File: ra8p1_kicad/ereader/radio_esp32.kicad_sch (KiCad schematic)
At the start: 22 parts, among them U3 ESP32-C6-WROOM-1-N8, U4 TPS22917DBVT, U5 TXU0304PWR, U6 TPS389001DSET, U7 SN74LVC1G97DBVR

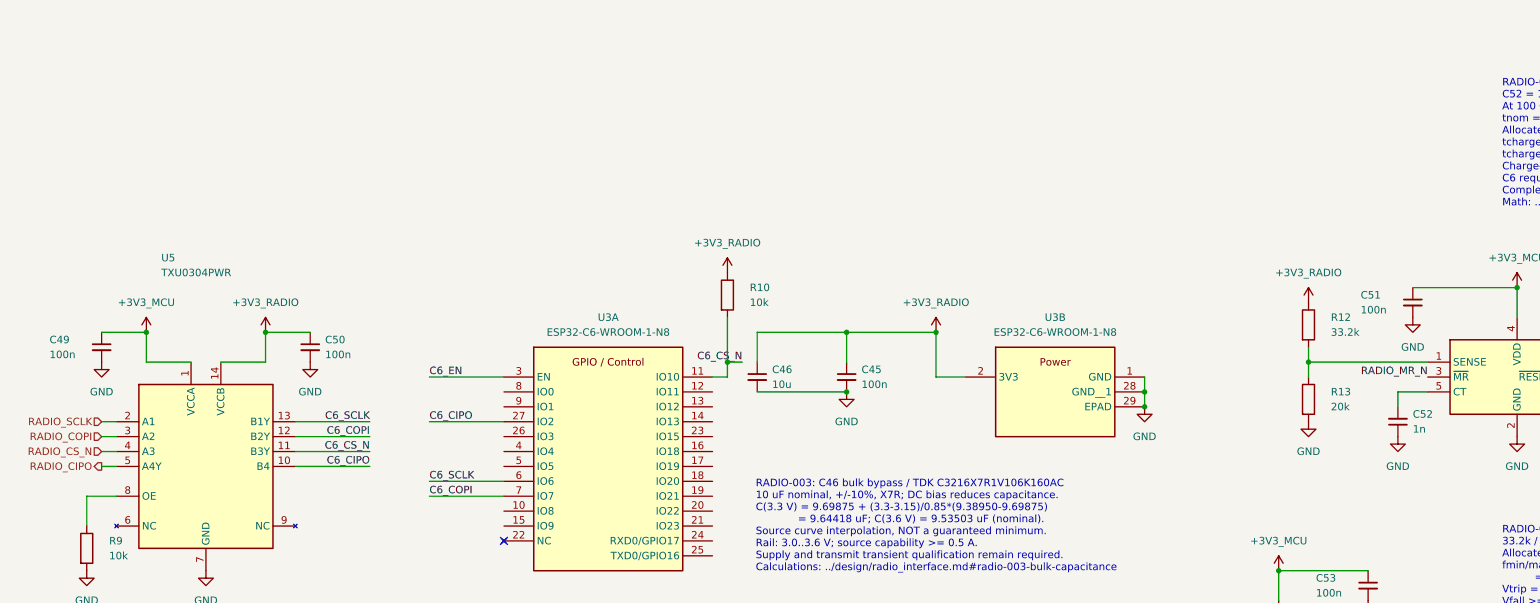
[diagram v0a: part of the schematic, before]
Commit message: Add radio SPI enable arbitration and linked DC calculations
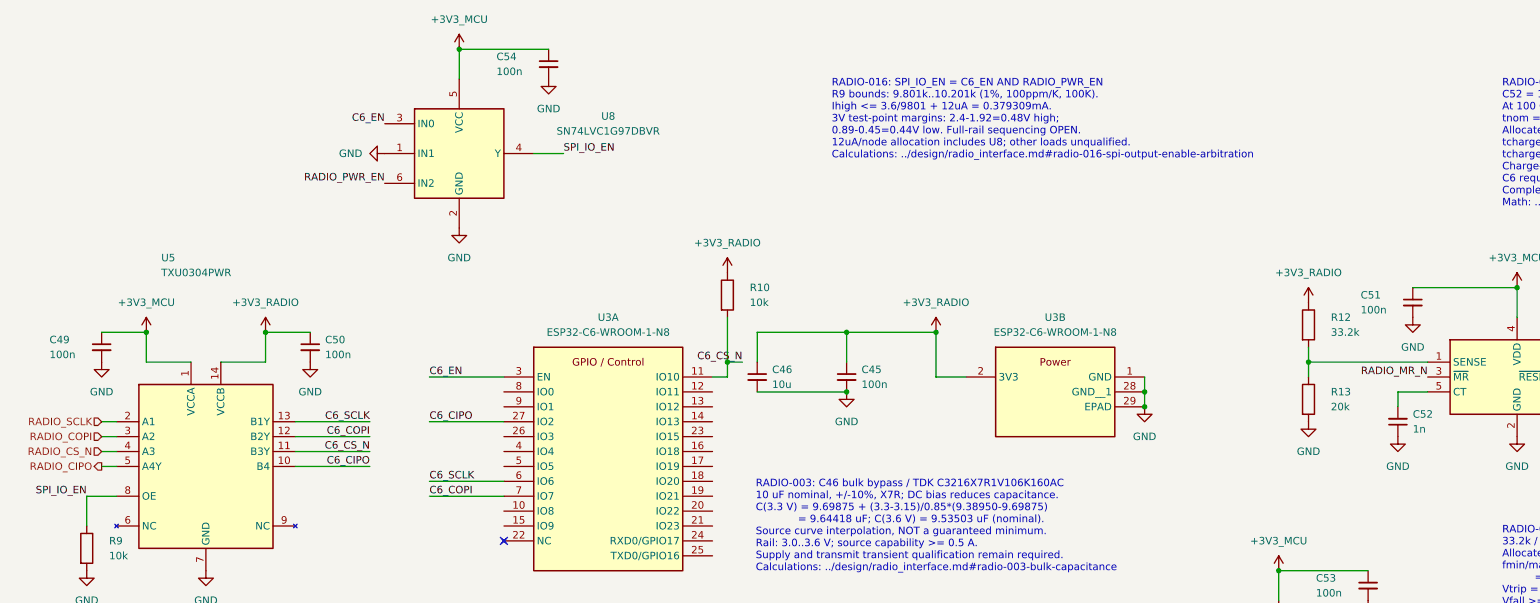
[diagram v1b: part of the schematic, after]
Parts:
- added C54: 100n, symbol Device:C_Small
- added U8: SN74LVC1G97DBVR, symbol 74xGxx:74LVC1G97
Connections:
- net +3V3_MCU: now also C54.1, U8.5 (VCC)
- net C6_EN: now also U8.3 (IN0)
- net GND: now also C54.2, U8.1 (IN1), U8.2 (GND)
- net RADIO_PWR_EN: now also U8.6 (IN2)
- net SPI_IO_EN: now reaches R9.1, U5.8 (OE)
- net SPI_IO_EN: now also U8.4 (Y)
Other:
- note added: "RADIO-016: SPI_IO_EN = C6_EN AND RADIO_PWR_EN R9 bounds: 9.801k..10.201k (1%, 100ppm/K, 100K). Ihigh <= 3.6/9801 + 12uA = 0.379309mA. 3V test-point margins: 2.4-1.92=0.48V high; 0.89-0.45=0.44V low. Full-rail sequencing OPEN. 12uA/node allocation includes U8; other loads unqualified. Calculations: ../design/radio_interface.md#radio-016-spi-output-enable-arbitration"

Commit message: Add ESP32 boot and debug strap bias with verified calculations
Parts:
- added R15, R16, R17: 10k, symbol Device:R
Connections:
- net +3V3_RADIO: now also R15.1, R16.1, R17.1
- net C6_GPIO8: now reaches U3.10 (IO8)
- net C6_GPIO8: now also R15.2
- net C6_BOOT_N: now reaches U3.15 (IO9)
- net C6_BOOT_N: now also R16.2
- net C6_GPIO15: now reaches U3.23 (IO15)
- net C6_GPIO15: now also R17.2
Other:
- note added: "RADIO-017: R15/R16/R17 boot/debug strap pull-ups to switched radio rail. Flash boot: GPIO9=1. Download: GPIO8=1, GPIO9=0; recovery driver not yet fitted. GPIO15=1 selects USB JTAG with applicable eFuses; retain straps >=3ms after EN rises. Rmin/max=10k*(1+/-1%)*(1+/-100ppm/K*100K)=9801/10201 ohm. At 3.3V: Vhigh>=3.3-12uA*10201=3.177588V; VIH=2.475V; margin=0.702588V. External low-state current<=3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"

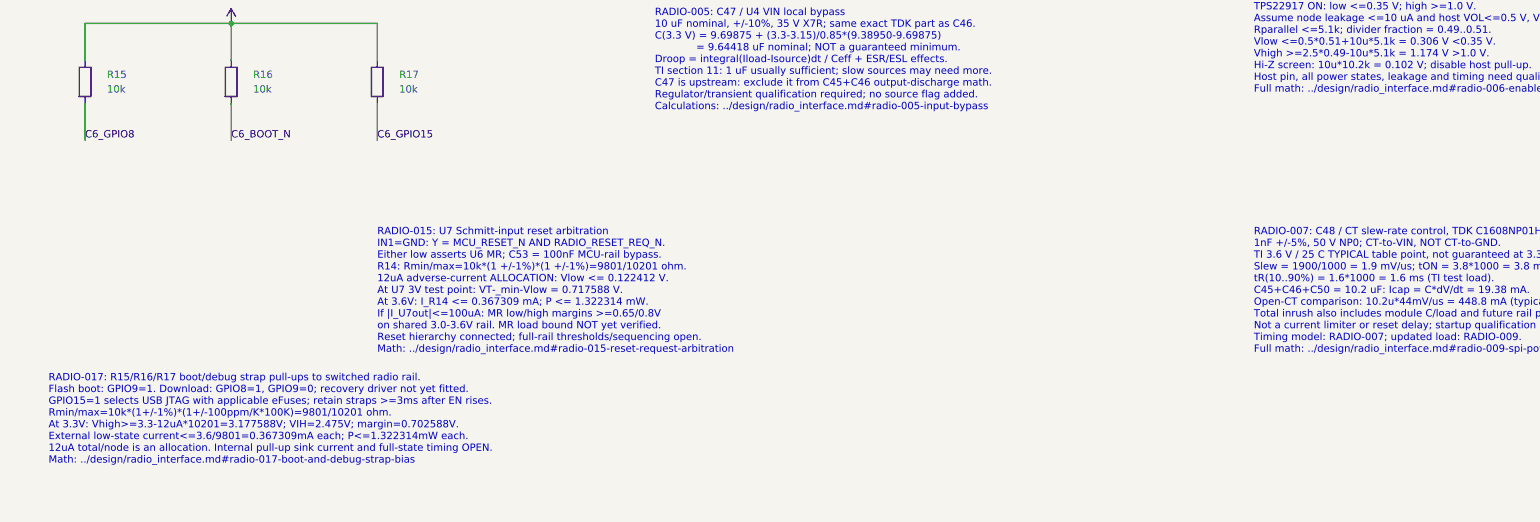
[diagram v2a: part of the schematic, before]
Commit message: Add sourced manual radio BOOT switch and recovery timing contract
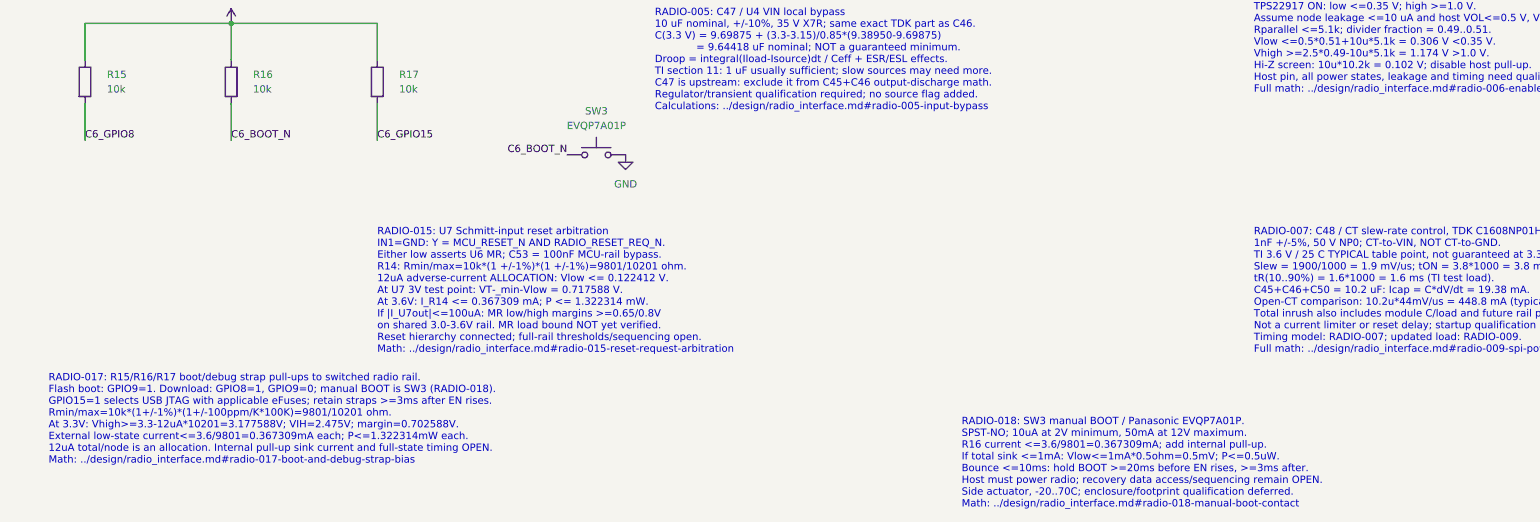
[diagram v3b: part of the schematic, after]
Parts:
- added SW3: EVQP7A01P, symbol Switch:SW_Push
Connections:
- net C6_BOOT_N: now also SW3.1
- net GND: now also SW3.2
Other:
- note added: "RADIO-017: R15/R16/R17 boot/debug strap pull-ups to switched radio rail. Flash boot: GPIO9=1. Download: GPIO8=1, GPIO9=0; manual BOOT is SW3 (RADIO-018). GPIO15=1 selects USB JTAG with applicable eFuses; retain straps >=3ms after EN rises. Rmin/max=10k*(1+/-1%)*(1+/-100ppm/K*100K)=9801/10201 ohm. At 3.3V: Vhigh>=3.3-12uA*10201=3.177588V; VIH=2.475V; margin=0.702588V. External low-state current<=3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"
- note added: "RADIO-018: SW3 manual BOOT / Panasonic EVQP7A01P. SPST-NO; 10uA at 2V minimum, 50mA at 12V maximum. R16 current <=3.6/9801=0.367309mA; add internal pull-up. If total sink <=1mA: Vlow<=1mA*0.5ohm=0.5mV; P<=0.5uW. Bounce <=10ms: hold BOOT >=20ms before EN rises, >=3ms after. Host must power radio; recovery data access/sequencing remain OPEN. Side actuator, -20..70C; enclosure/footprint qualificatio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"
- note removed: "RADIO-017: R15/R16/R17 boot/debug strap pull-ups to switched radio rail. Flash boot: GPIO9=1. Download: GPIO8=1, GPIO9=0; recovery driver not yet fitted. GPIO15=1 selects USB JTAG with applicable eFuses; retain straps >=3ms after EN rises. Rmin/max=10k*(1+/-1%)*(1+/-100ppm/K*100K)=9801/10201 ohm. At 3.3V: Vhigh>=3.3-12uA*10201=3.177588V; VIH=2.475V; margin=0.702588V. External low-state current<=3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"

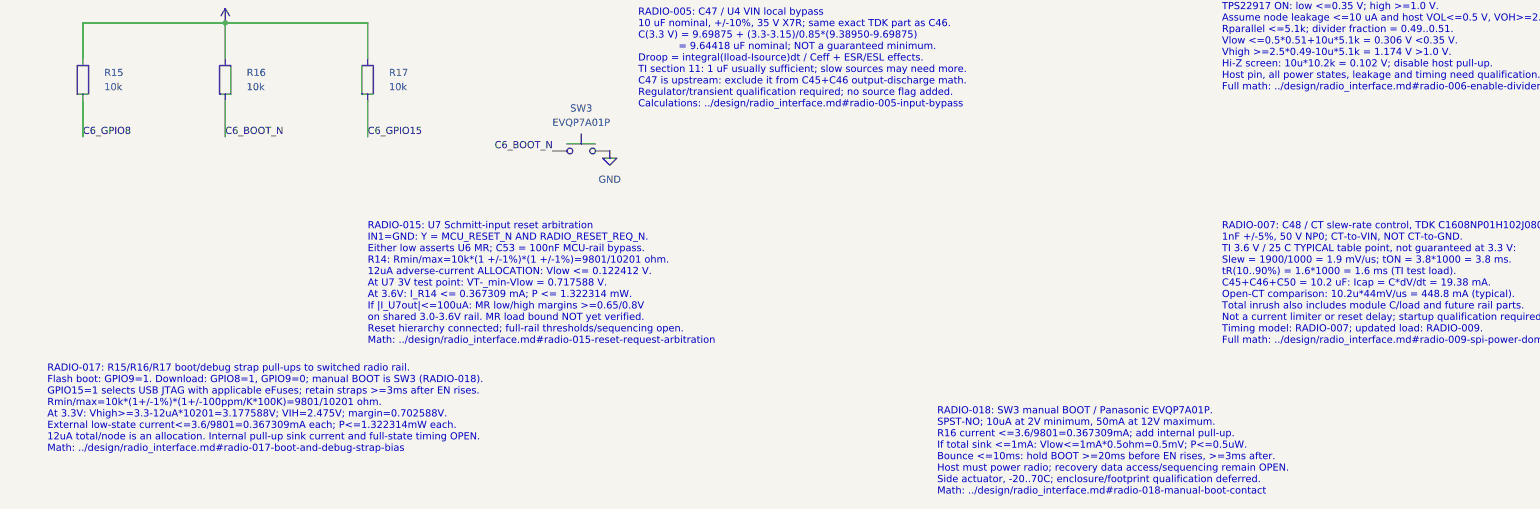
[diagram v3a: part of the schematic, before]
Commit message: Replace engineering BOOT and reset switches with internal service pads
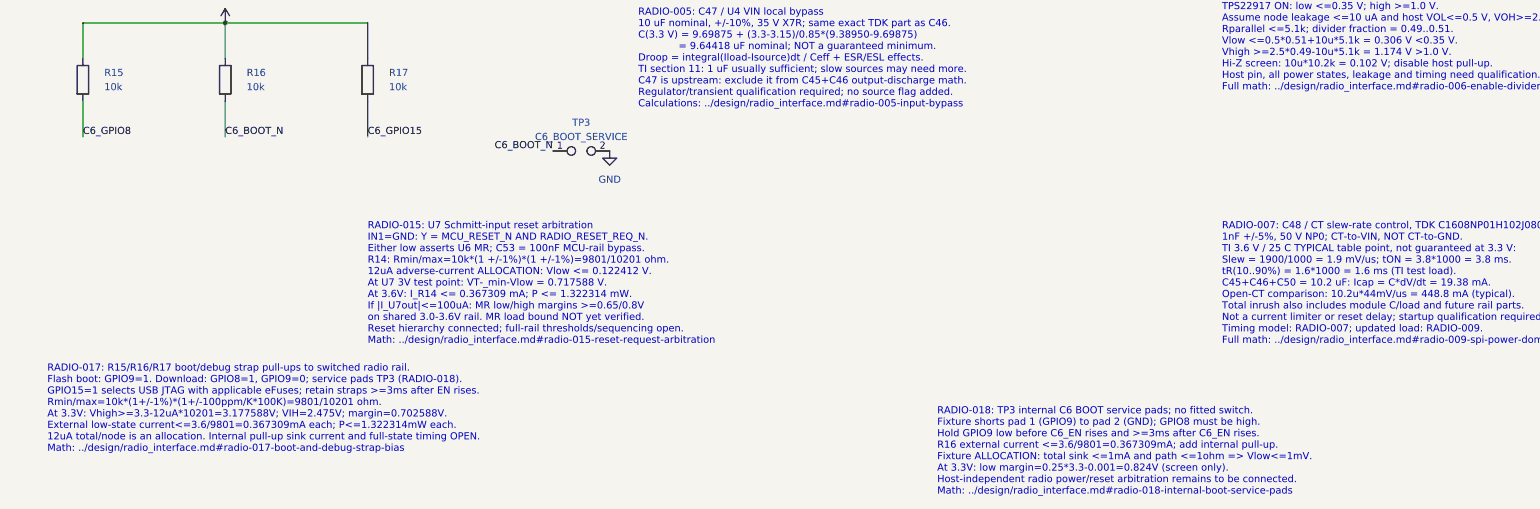
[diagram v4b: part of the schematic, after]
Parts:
- TP3: renamed from SW3; value EVQP7A01P -> C6_BOOT_SERVICE; symbol Switch:SW_Push -> Connector:TestPoint_2Pole; DigiKey_Part_Number P16763CT-ND -> (none); DigiKey_URL https://www.digikey.com/en/products/detail/panasonic-indust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 -> (none); Manufacturer_Name Panasonic Industry -> (none); Manufacturer_Part_Number EVQP7A01P -> (none); Procurement_Status Selected - primary electrical ratings and sourcing checked;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 -> (none); Selection_Basis RADIO-018: low-current SPST-NO BOOT contact to GND. R16 ext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 -> (none); Sourcing_Snapshot 2026-09-07 DigiKey indexed: Active; 32562 in stock; USD CT 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 -> (none); now left out of the parts list
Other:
- note added: "RADIO-017: R15/R16/R17 boot/debug strap pull-ups to switched radio rail. Flash boot: GPIO9=1. Download: GPIO8=1, GPIO9=0; service pads TP3 (RADIO-018). GPIO15=1 selects USB JTAG with applicable eFuses; retain straps >=3ms after EN rises. Rmin/max=10k*(1+/-1%)*(1+/-100ppm/K*100K)=9801/10201 ohm. At 3.3V: Vhigh>=3.3-12uA*10201=3.177588V; VIH=2.475V; margin=0.702588V. External low-state current<=3.6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"
- note added: "RADIO-018: TP3 internal C6 BOOT service pads; no fitted switch. Fixture shorts pad 1 (GPIO9) to pad 2 (GND); GPIO8 must be high. Hold GPIO9 low before C6_EN rises and >=3ms after C6_EN rises. R16 external current <=3.6/9801=0.367309mA; add internal pull-up. Fixture ALLOCATION: total sink <=1mA and path <=1ohm => Vlow<=1mV. At 3.3V: low margin=0.25*3.3-0.001=0.824V (screen only). Host-independent 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"
- note removed: "RADIO-017: R15/R16/R17 boot/debug strap pull-ups to switched radio rail. Flash boot: GPIO9=1. Download: GPIO8=1, GPIO9=0; manual BOOT is SW3 (RADIO-018). GPIO15=1 selects USB JTAG with applicable eFuses; retain straps >=3ms after EN rises. Rmin/max=10k*(1+/-1%)*(1+/-100ppm/K*100K)=9801/10201 ohm. At 3.3V: Vhigh>=3.3-12uA*10201=3.177588V; VIH=2.475V; margin=0.702588V. External low-state current<=3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"
- note removed: "RADIO-018: SW3 manual BOOT / Panasonic EVQP7A01P. SPST-NO; 10uA at 2V minimum, 50mA at 12V maximum. R16 current <=3.6/9801=0.367309mA; add internal pull-up. If total sink <=1mA: Vlow<=1mA*0.5ohm=0.5mV; P<=0.5uW. Bounce <=10ms: hold BOOT >=20ms before EN rises, >=3ms after. Host must power radio; recovery data access/sequencing remain OPEN. Side actuator, -20..70C; enclosure/footprint qualificatio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"
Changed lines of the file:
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@@
 		)
 	)
-	(text "RADIO-018: SW3 manual BOOT / Panasonic EVQP7A01P.\nSPST-NO; 10uA at 2V minimum, 50mA at 12V maximum.\nR16 current <=3.6/9801=0.367309mA; add internal pull-up.\nIf total sink <=1mA: Vlow<=1mA*0.5ohm=0.5mV; P<=0.5uW.\nBounce <=10ms: hold BOOT >=20ms before EN rises, >=3ms after.\nHost must power radio; recovery data access/sequencing remain OPEN.\nSide actuator, -20..70C; enclosure/footprint qualification deferred.\nMath: ../design/radio_interface.md#radio-018-manual-boot-contact"
+	(text "RADIO-018: TP3 internal C6 BOOT service pads; no fitted switch.\nFixture shorts pad 1 (GPIO9) to pad 2 (GND); GPIO8 must be high.\nHold GPIO9 low before C6_EN rises and >=3ms after C6_EN rises.\nR16 external current <=3.6/9801=0.367309mA; add internal pull-up.\nFixture ALLOCATION: total sink <=1mA and path <=1ohm => Vlow<=1mV.\nAt 3.3V: low margin=0.25*3.3-0.001=0.824V (screen only).\nHost-independent radio power/reset arbitration remains to be connected.\nMath: ../design/radio_interface.md#radio-018-internal-boot-service-pads	"
 		(exclude_from_sim no)
 		(at 177.8 261.62 0)
@@
 		)
 	)
-	(text "RADIO-017: R15/R16/R17 boot/debug strap pull-ups to switched radio rail.\nFlash boot: GPIO9=1. Download: GPIO8=1, GPIO9=0; manual BOOT is SW3 (RADIO-018).\nGPIO15=1 selects USB JTAG with applicable eFuses; retain straps >=3ms after EN rises.\nRmin/max=10k*(1+/-1%)*(1+/-100ppm/K*100K)=9801/10201 ohm.\nAt 3.3V: Vhigh>=3.3-12uA*10201=3.177588V; VIH=2.475V; margin=0.702588V.\nExternal low-state current<=3.6/9801=0.367309mA each; P<=1.322314mW each.\n12uA total/node is an allocation. Internal pull-up sink current and full-state timing OPEN.\nMath: ../design/radio_interface.md#radio-017-boot-and-debug-strap-bias"
+	(text "RADIO-017: R15/R16/R17 boot/debug strap pull-ups to switched radio rail.\nFlash boot: GPIO9=1. Download: GPIO8=1, GPIO9=0; service pads TP3 (RADIO-018).\nGPIO15=1 selects USB JTAG with applicable eFuses; retain straps >=3ms after EN rises.\nRmin/max=10k*(1+/-1%)*(1+/-100ppm/K*100K)=9801/10201 ohm.\nAt 3.3V: Vhigh>=3.3-12uA*10201=3.177588V; VIH=2.475V; margin=0.702588V.\nExternal low-state current<=3.6/9801=0.367309mA each; P<=1.322314mW each.\n12uA total/node is an allocation. Internal pull-up sink current and full-state timing OPEN.\nMath: ../design/radio_interface.md#radio-017-boot-and-debug-strap-bias	"
 		(exclude_from_sim no)
 		(at 19.05 254 0)
@@
 	)
 	(symbol
-		(lib_id "Switch:SW_Push")
+		(lib_id "Connector:TestPoint_2Pole")
 		(at 114.3 215.9 0)
 		(unit 1)
 		(body_style 1)
 		(exclude_from_sim no)
-		(in_bom yes)
+		(in_bom no)
 		(on_board yes)
-		(in_pos_files yes)
+		(in_pos_files no)
 		(dnp no)
 		(fields_autoplaced yes)
-		(property "Reference" "SW3"
-			(at 114.3 208.28 0)
-			(show_name no)
-			(do_not_autoplace no)
-			(effects
-				(font
-					(size 1.27 1.27)
-				)
-			)
-		)
-		(property "Value" "EVQP7A01P"
-			(at 114.3 210.82 0)
-			(show_name no)
-			(do_not_autoplace no)
-			(effects
-				(font
-					(size 1.27 1.27)
-				)
-			)
-		)
-		(property "Footprint" ""
+		(property "Reference" "TP3"
 			(at 114.3 210.82 0)
-			(hide yes)
 			(show_name no)
 			(do_not_autoplace no)
@@
 			)
 		)
-		(property "Datasheet" "https://industrial.panasonic.com/cdbs/www-data/pdf/ATK0000/ATK0000C378.pdf"
-			(at 114.3 210.82 0)
-			(hide yes)
+		(property "Value" "C6_BOOT_SERVICE"
+			(at 114.3 213.36 0)
 			(show_name no)
 			(do_not_autoplace no)
@@
 			)
 		)
-		(property "Description" "RADIO-018: Panasonic EVQP7A01P SPST-NO BOOT switch, C6_BOOT_N to GND. 10uA/2V minimum resistive load; 50mA/12V maximum; side actuation; -20..70C."
-			(at 114.3 215.9 0)
-			(hide yes)
-			(show_name no)
-			(do_not_autoplace no)
-			(effects
-				(font
-					(size 1.27 1.27)
-				)
-			)
-		)
-		(property "Manufacturer_Name" "Panasonic Industry"
-			(at 114.3 215.9 0)
-			(hide yes)
-			(show_name no)
-			(do_not_autoplace no)
-			(effects
-				(font
-					(size 1.27 1.27)
-				)
-			)
-		)
-		(property "Manufacturer_Part_Number" "EVQP7A01P"
-			(at 114.3 215.9 0)
-			(hide yes)
-			(show_name no)
-			(do_not_autoplace no)
-			(effects
-				(font
-					(size 1.27 1.27)
-				)
-			)
-		)
-		(property "DigiKey_Part_Number" "P16763CT-ND"
-			(at 114.3 215.9 0)
-			(hide yes)
-			(show_name no)
-			(do_not_autoplace no)
-			(effects
-				(font
-					(size 1.27 1.27)
-				)
-			)
-		)
-		(property "DigiKey_URL" "https://www.digikey.com/en/products/detail/panasonic-industry/EVQ-P7A01P/4429447"
-			(at 114.3 215.9 0)
-			(hide yes)
-			(show_name no)
-			(do_not_autoplace no)
-			(effects
-				(font
-					(size 1.27 1.27)
-				)
-			)
-		)
-		(property "Selection_Basis" "RADIO-018: low-current SPST-NO BOOT contact to GND. R16 external current <=0.367309mA; contact R<=0.5ohm. 10ms bounce; hold before reset release. -20..70C, side actuator; mechanics deferred."
+		(property "Footprint" ""
 			(at 114.3 215.9 0)
 			(hide yes)
@@
 			)
 		)
-		(property "Sourcing_Snapshot" "2026-09-07 DigiKey indexed: Active; 32562 in stock; USD CT qty1 0.28 / 10 0.248 / 100 0.2076; 18-week lead. Dated snapshot, not order quote."
+		(property "Datasheet" ""
 			(at 114.3 215.9 0)
 			(hide yes)
@@
 			)
 		)
-		(property "Procurement_Status" "Selected - primary electrical ratings and sourcing checked; full reset/recovery qualification open; footprint and actuator access deferred."
+		(property "Description" "Internal paired copper service pads: 1=C6_BOOT_N, 2=GND. Fixture pulls GPIO9 low for ROM download; no fitted switch. RADIO-018."
 			(at 114.3 215.9 0)
 			(hide yes)
@@
 			(project "ereader_rev1"
 				(path "/0586cc51-9c57-495b-a0c9-c29ba0d48166/9b84c337-6879-4714-899e-3993bcc30b88"
-					(reference "SW3")
+					(reference "TP3")
 					(unit 1)
 				)
